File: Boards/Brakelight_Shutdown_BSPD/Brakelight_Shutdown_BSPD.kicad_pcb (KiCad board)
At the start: 2 copper layers, 60.3 x 91.4 mm, 91 parts, among them IC1 ATMEGA16M1, J1 MM_F_RA_06, J2 MM_F_RA_20, J3 CONN_02X03, Q1 SSM3K333R, Q2 SSM3K333R, Q3 SSM3K333R, Q4 SSM3K333R, Q5 SSM3K333R, Q6 SSM3K333R, Q7 SSM3K333R, U1 SN74LVC1G08, U2 MCP6001, U3 CAN_Transceiver, U4 TPS561201, U5 SN74LVC1G02, U6 SN74LVC1G02, U7 MCP6001, Y1 Crystal_SMD

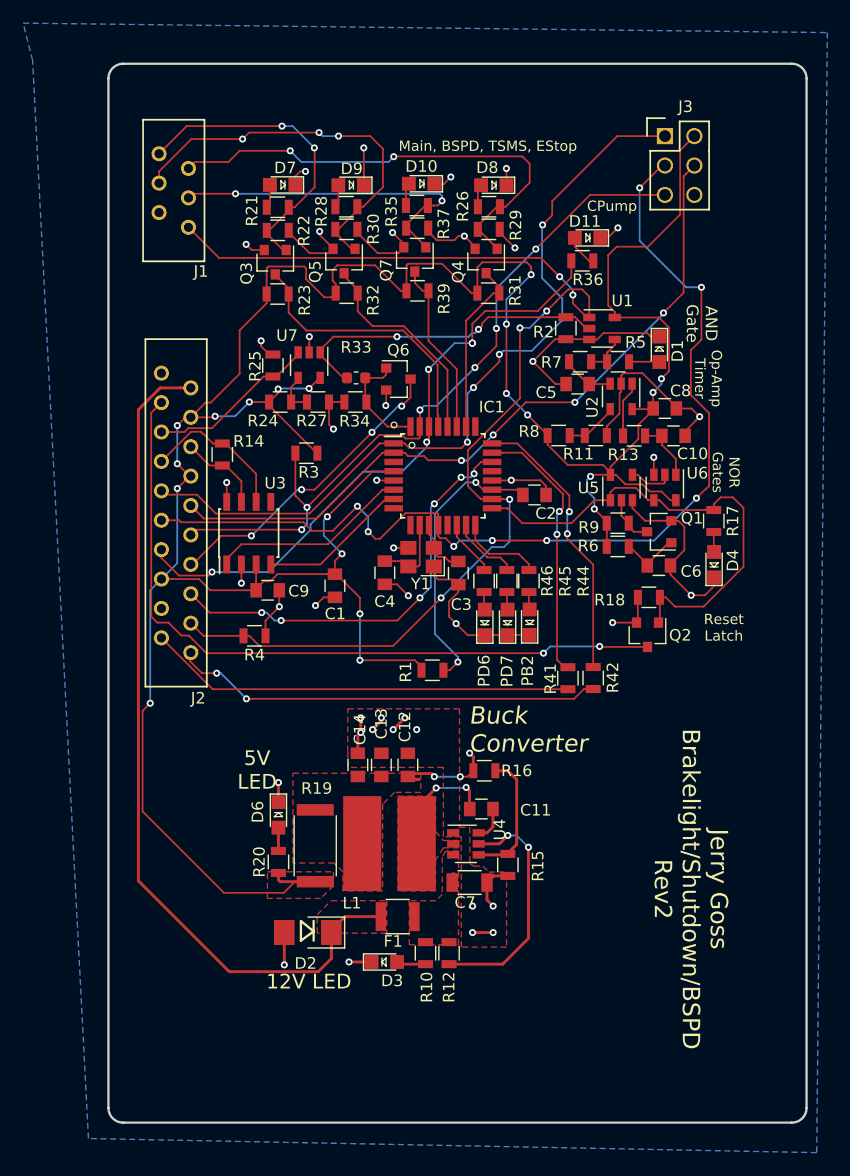
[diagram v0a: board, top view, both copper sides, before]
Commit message: Moving micromatch connectors closer to edge and reducing overall size of the board (edgecuts)
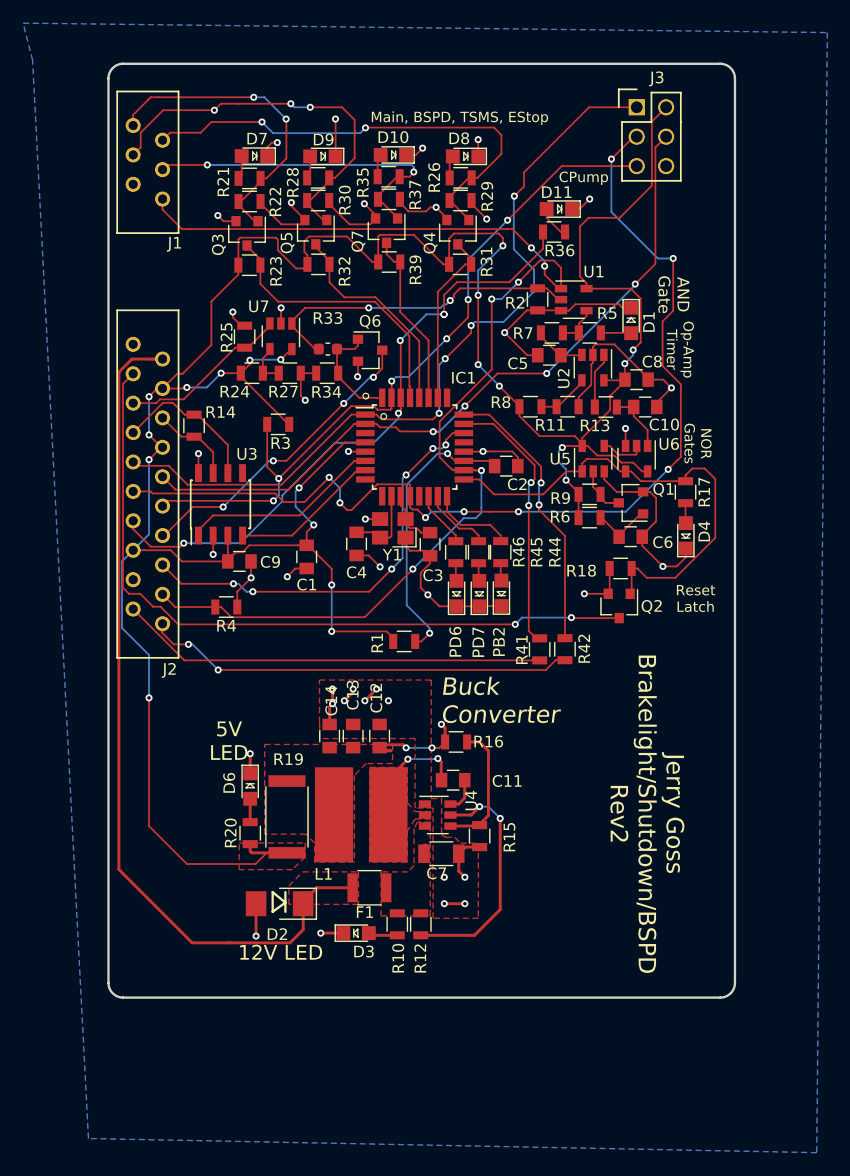
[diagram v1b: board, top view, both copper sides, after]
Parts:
- moved C11 3.48 mm to (190.3, 108.9)
- moved D3 3.48 mm to (181.9, 122.1)
- moved J2 3.48 mm to (162.7, 76.3)
- moved R10 3.48 mm to (185.5, 121.3)
- moved R11 3.48 mm to (200.2, 76.6)
- moved R12 3.48 mm to (187.5, 121.3)
- moved R14 3.48 mm to (167.9, 78.2)
- moved R3 3.48 mm to (175.2, 78.1)
- moved R31 3.48 mm to (190.9, 64.3)
- moved R32 3.48 mm to (178.7, 64.3)
- moved R5 3.48 mm to (202.1, 70.2)
- moved R6 3.48 mm to (202.1, 86.2)
- moved R7 3.48 mm to (198.8, 70.2)
- moved R8 3.48 mm to (197.0, 76.6)
- moved U3 3.48 mm to (170.2, 85.0)
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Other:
- board size 60.3 x 91.4 mm -> 54.1 x 80.6 mm
